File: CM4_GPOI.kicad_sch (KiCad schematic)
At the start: 28 parts, among them J4 Conn_02x04_Odd_Even, J5 61900419521, M2 CM4-GPIO, SW1 SW_Push, U11 EMC2301, U5 74LVC1G07SE-7, U9 SLB9672XU20FW1612XTMA1

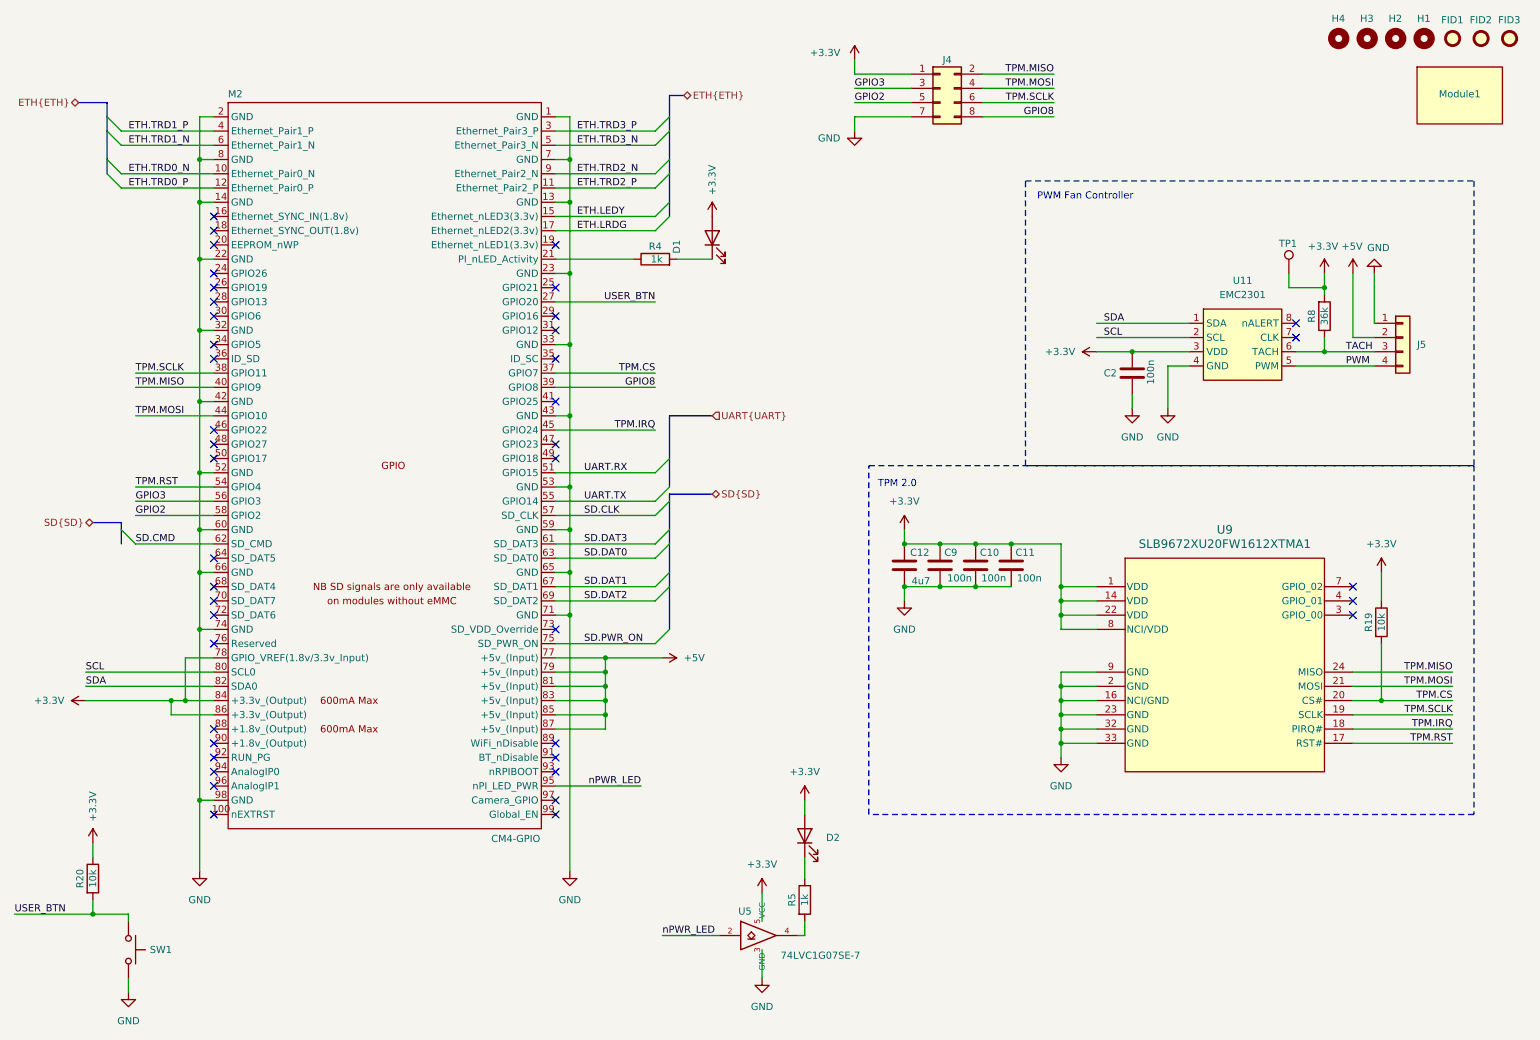
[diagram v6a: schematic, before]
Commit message: feat: adjust pin header
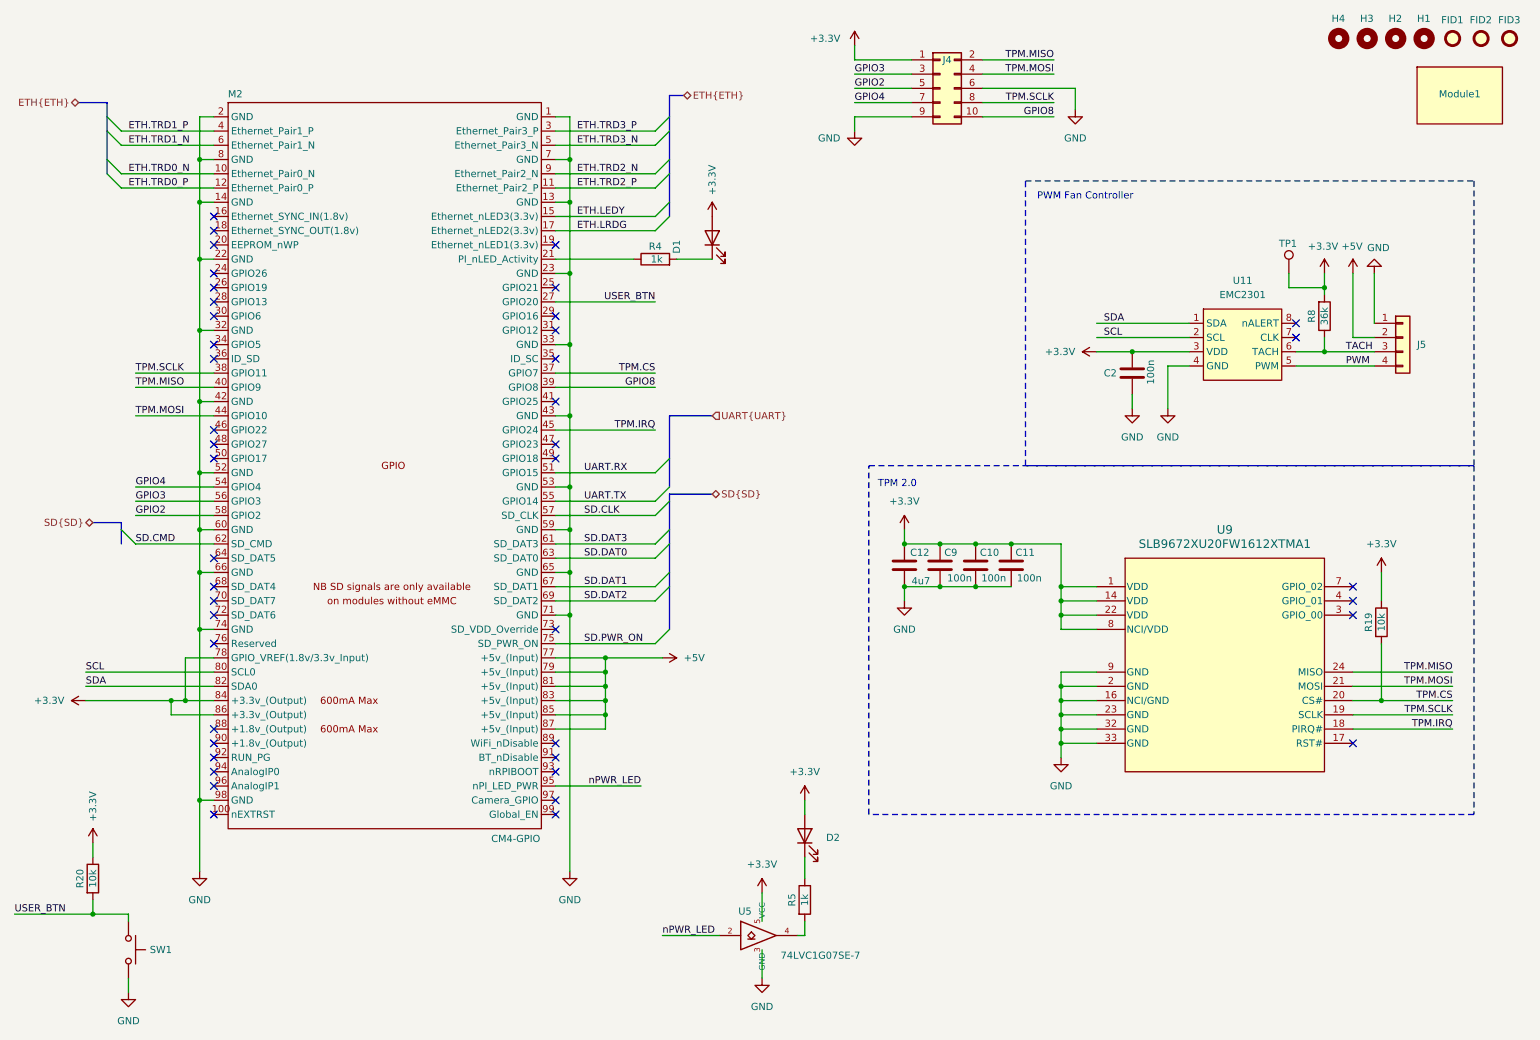
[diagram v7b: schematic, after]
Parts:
- J4: footprint Hardware Components:Conn_PinHeader_2x04_P2.54mm_Vertical -> Hardware Components:Conn_PinHeader_2x05_P2.54mm_Vertical; symbol Hardware Components:Conn_PinHeader_2x04_P2.54mm_Vertical -> Hardware Components:Conn_PinHeader_2x05_P2.54mm_Vertical; JLCPCB Part # C492421 -> C492422; MPN PZ254V-12-8P -> PZ254V-12-10P
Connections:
- net GND: now also J4.6 (Pin_6), J4.9 (Pin_9); no longer J4.7 (Pin_7)
- net GPIO8: now also J4.10 (Pin_10); no longer J4.8 (Pin_8)
- net TPM.SCLK: now also J4.8 (Pin_8); no longer J4.6 (Pin_6)
- net TPM.RST: no longer names the net of U9.17 (RST#)
- net TPM.RST: no longer M2.54 (GPIO4)
- new net GPIO4: J4.7 (Pin_7), M2.54 (GPIO4)
- no-connect marks 42 -> 43
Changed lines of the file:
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@@
 	)
 	(no_connect
+		(at 254 144.78)
+	)
+	(no_connect
 		(at 50.8 127)
 	)
@@
 	(wire
 		(pts
-			(xy 165.1 25.4) (xy 175.26 25.4)
+			(xy 165.1 22.86) (xy 175.26 22.86)
 		)
 		(stroke
@@
 	(wire
 		(pts
-			(xy 254 144.78) (xy 271.78 144.78)
-		)
-		(stroke
-			(width 0)
-			(type default)
-		)
-	)
-	(wire
-		(pts
 			(xy 156.21 165.1) (xy 156.21 168.91)
 		)
@@
 	(wire
 		(pts
-			(xy 114.3 99.06) (xy 114.3 106.68)
+			(xy 204.47 31.75) (xy 204.47 27.94)
 		)
 		(stroke
@@
 	(wire
 		(pts
-			(xy 111.76 96.52) (xy 129.54 96.52)
+			(xy 114.3 99.06) (xy 114.3 106.68)
 		)
 		(stroke
@@
 	(wire
 		(pts
-			(xy 114.3 114.3) (xy 114.3 121.92)
+			(xy 111.76 96.52) (xy 129.54 96.52)
 		)
 		(stroke
@@
 	(wire
 		(pts
-			(xy 187.96 27.94) (xy 200.66 27.94)
+			(xy 114.3 114.3) (xy 114.3 121.92)
 		)
 		(stroke
@@
 	(wire
 		(pts
+			(xy 187.96 27.94) (xy 204.47 27.94)
+		)
+		(stroke
+			(width 0)
+			(type default)
+		)
+	)
+	(wire
+		(pts
 			(xy 201.93 142.24) (xy 201.93 144.78)
 		)
@@
 		)
 	)
+	(wire
+		(pts
+			(xy 165.1 30.48) (xy 175.26 30.48)
+		)
+		(stroke
+			(width 0)
+			(type default)
+		)
+	)
 	(bus
 		(pts
@@
 	(wire
 		(pts
-			(xy 165.1 25.4) (xy 165.1 22.86)
+			(xy 165.1 22.86) (xy 165.1 20.32)
 		)
 		(stroke
@@
 	(wire
 		(pts
-			(xy 248.92 72.39) (xy 248.92 74.93)
+			(xy 187.96 22.86) (xy 200.66 22.86)
 		)
 		(stroke
@@
 	(wire
 		(pts
-			(xy 165.1 30.48) (xy 175.26 30.48)
+			(xy 248.92 72.39) (xy 248.92 74.93)
 		)
 		(stroke
@@
 	(wire
 		(pts
-			(xy 165.1 35.56) (xy 165.1 33.02)
+			(xy 165.1 27.94) (xy 175.26 27.94)
 		)
 		(stroke
@@
 	(wire
 		(pts
-			(xy 187.96 25.4) (xy 200.66 25.4)
+			(xy 165.1 35.56) (xy 165.1 33.02)
 		)
 		(stroke
@@
 	(wire
 		(pts
-			(xy 165.1 27.94) (xy 175.26 27.94)
+			(xy 165.1 25.4) (xy 175.26 25.4)
 		)
 		(stroke
@@
 		)
 	)
+	(wire
+		(pts
+			(xy 187.96 25.4) (xy 200.66 25.4)
+		)
+		(stroke
+			(width 0)
+			(type default)
+		)
+	)
 	(bus
 		(pts
@@
 	)
 	(label "GPIO2"
-		(at 165.1 30.48 0)
+		(at 165.1 27.94 0)
 		(effects
 			(font
@@
 		)
 	)
-	(label "TPM.MOSI"
-		(at 200.66 27.94 180)
-		(effects
-			(font
-				(size 1.27 1.27)
-			)
-			(justify right bottom)
-		)
-	)
 	(label "SCL"
 		(at 27.94 132.08 0)
@@
 		)
 	)
-	(label "TPM.RST"
-		(at 271.78 144.78 180)
+	(label "GPIO4"
+		(at 165.1 30.48 0)
 		(effects
 			(font
 				(size 1.27 1.27)
 			)
-			(justify right bottom)
+			(justify left bottom)
 		)
 	)
 	(label "GPIO3"
-		(at 165.1 27.94 0)
+		(at 165.1 25.4 0)
 		(effects
 			(font
@@
 		)
 	)
-	(label "TPM.MISO"
-		(at 200.66 25.4 180)
-		(effects
-			(font
-				(size 1.27 1.27)
-			)
-			(justify right bottom)
-		)
-	)
 	(label "ETH.LEDY"
 		(at 115.57 50.8 0)
@@
 		)
 	)
-	(label "TPM.RST"
+	(label "GPIO4"
 		(at 36.83 99.06 0)
 		(effects
@@
 		)
 	)
+	(label "TPM.MOSI"
+		(at 200.66 25.4 180)
+		(effects
+			(font
+				(size 1.27 1.27)
+			)
+			(justify right bottom)
+		)
+	)
+	(label "TPM.MISO"
+		(at 200.66 22.86 180)
+		(effects
+			(font
+				(size 1.27 1.27)
+			)
+			(justify right bottom)
+		)
+	)
 	(label "ETH.TRD0_N"
 		(at 35.56 43.18 0)
@@
 	)
 	(symbol
-		(lib_id "Hardware Components:Conn_PinHeader_2x04_P2.54mm_Vertical")
+		(lib_id "Hardware Components:Conn_PinHeader_2x05_P2.54mm_Vertical")
 		(at 180.34 27.94 0)
 		(unit 1)
@@
 			)
 		)
-		(property "Footprint" "Hardware Components:Conn_PinHeader_2x04_P2.54mm_Vertical"
+		(property "Footprint" "Hardware Components:Conn_PinHeader_2x05_P2.54mm_Vertical"
 			(at 180.34 27.94 0)
 			(effects
@@
 			)
 		)
-		(property "Datasheet" "https://jlcpcb.com/api/file/downloadByFileSystemAccessId/8588888830455779328"
+		(property "Datasheet" "https://jlcpcb.com/api/file/downloadByFileSystemAccessId/8588888831508008960"
 			(at 180.34 27.94 0)
 			(effects
@@
 			)
 		)
-		(property "Description" "Direct Insert Policy 2.5mm 8P 6mm -40℃~+105℃ 3mm 2.54mm Double Row Black Brass 2x4P 2.54mm Plugin,P=2.54mm Pin Headers ROHS"
+		(property "Description" "-40℃~+105℃ 10P 2 2.54mm 2.54mm 2.5mm 2x5P 3mm 6mm Black Brass Pin Header Through Hole Plugin,P=2.54mm Pin Headers ROHS"
 			(at 180.34 27.94 0)
 			(effects
@@
 			)
 		)
-		(property "MPN" "PZ254V-12-8P"
+		(property "MPN" "PZ254V-12-10P"
 			(at 180.34 27.94 0)
 			(effects
@@
 			)
 		)
-		(property "JLCPCB Part #" "C492421"
+		(property "JLCPCB Part #" "C492422"
 			(at 180.34 27.94 0)
 			(effects
@@
 		(pin "7"
 		)
+		(pin "9"
+		)
+		(pin "10"
+		)
 		(instances
 			(project "HomeLabIO"
@@
 	)
 	(symbol
+		(lib_id "power:GND")
+		(at 204.47 31.75 0)
+		(unit 1)
+		(exclude_from_sim no)
+		(in_bom yes)
+		(on_board yes)
+		(dnp no)
+		(fields_autoplaced yes)
+		(property "Reference" "#PWR066"
+			(at 204.47 38.1 0)
+			(effects
+				(font
+					(size 1.27 1.27)
+				)
+				(hide yes)
+			)
+		)
+		(property "Value" "GND"
+			(at 204.47 36.83 0)
+			(effects
+				(font
+					(size 1.27 1.27)
+				)
+			)
+		)
+		(property "Footprint" ""
+			(at 204.47 31.75 0)
+			(effects
+				(font
+					(size 1.27 1.27)
+				)
+				(hide yes)
+			)
+		)
+		(property "Datasheet" ""
+			(at 204.47 31.75 0)
+			(effects
+				(font
+					(size 1.27 1.27)
+				)
+				(hide yes)
+			)
+		)
+		(property "Description" "Power symbol creates a global label with name \"GND\" , ground"
+			(at 204.47 31.75 0)
+			(effects
+				(font
+					(size 1.27 1.27)
+				)
+				(hide yes)
+			)
+		)
+		(pin "1"
+		)
+		(instances
+			(project "HomeLabIO"
+				(path "/938dda83-8624-4563-91c2-df725c684a81/ca370b1f-0541-49c0-b507-b29c9c38f03b"
+					(reference "#PWR066")
+					(unit 1)
+				)
+			)
+		)
+	)
+	(symbol
 		(lib_id "Hardware Components:Compute-Module-4_H1")
 		(at 273.05 29.21 0)
@@
 	(symbol
 		(lib_id "power:+3.3V")
-		(at 165.1 22.86 0)
+		(at 165.1 20.32 0)
 		(unit 1)
 		(exclude_from_sim no)
@@
 		(fields_autoplaced yes)
 		(property "Reference" "#PWR035"
-			(at 165.1 26.67 0)
+			(at 165.1 24.13 0)
 			(effects
 				(font
@@
 		)
 		(property "Value" "+3.3V"
-			(at 162.56 21.5901 0)
+			(at 162.56 19.0501 0)
 			(effects
 				(font
@@
 		)
 		(property "Footprint" ""
-			(at 165.1 22.86 0)
+			(at 165.1 20.32 0)
 			(effects
 				(font
@@
 		)
 		(property "Datasheet" ""
-			(at 165.1 22.86 0)
+			(at 165.1 20.32 0)
 			(effects
 				(font
@@
 		)
 		(property "Description" "Power symbol creates a global label with name \"+3.3V\""
-			(at 165.1 22.86 0)
+			(at 165.1 20.32 0)
 			(effects
 				(font
